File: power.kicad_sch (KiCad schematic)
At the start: 3 parts, among them U1 AP7363-33D-13

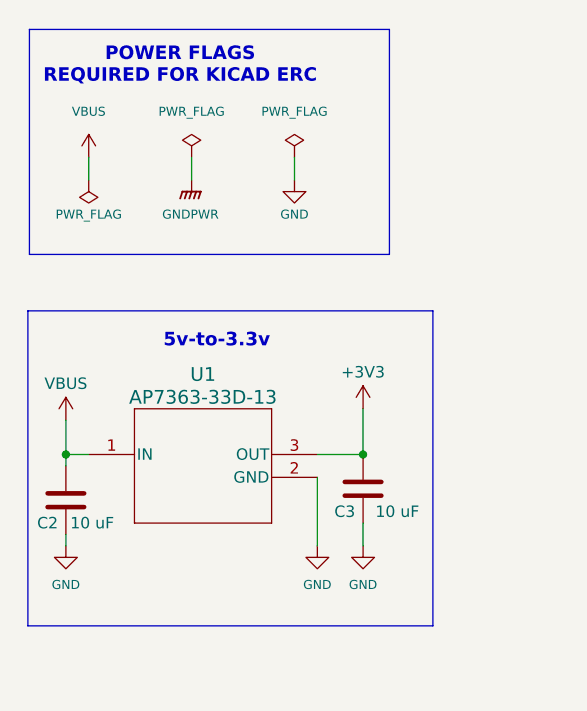
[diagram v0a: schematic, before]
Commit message: finished ERC, matched footprints, populated 3D models
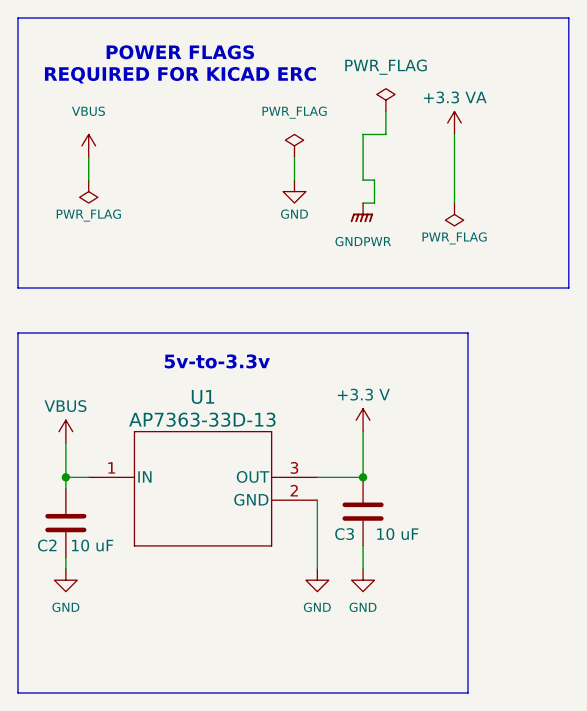
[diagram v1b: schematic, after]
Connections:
- net +3V3 renamed +3.3 V
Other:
- moved on the sheet: C2, C3, U1

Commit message: matched footprint name to name of component
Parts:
- U1: footprint AP7363_33D_13:TO252-3L_DIO -> AP7363_33D_13:AP7363-33D-13
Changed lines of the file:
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@@
 			)
 		)
-		(property "Footprint" "AP7363_33D_13:TO252-3L_DIO"
+		(property "Footprint" "AP7363_33D_13:AP7363-33D-13"
 			(at 12.446 69.088 0)
 			(effects

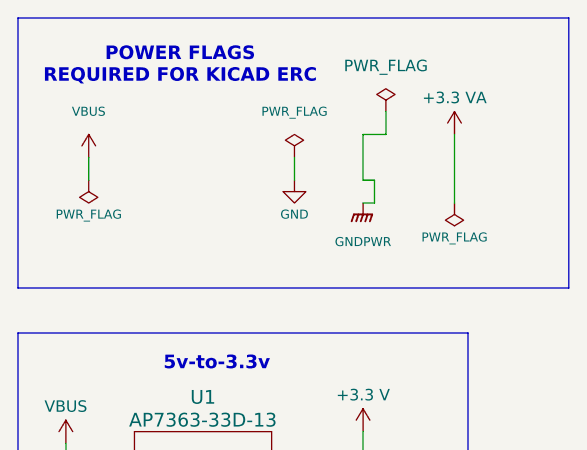
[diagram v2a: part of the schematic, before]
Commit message: removed manual switch
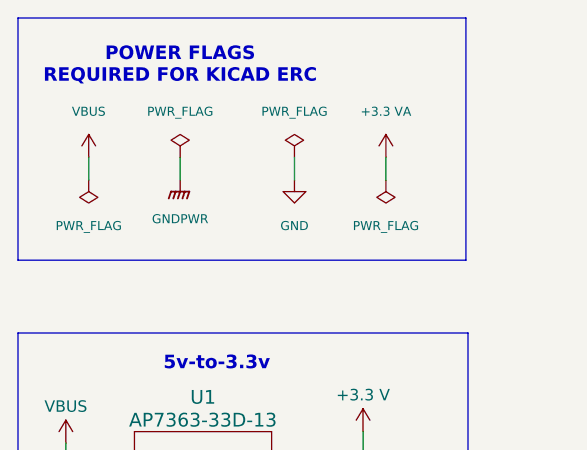
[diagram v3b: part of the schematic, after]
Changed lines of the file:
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@@
-	(wire
-		(pts
-			(xy 55.88 25.4) (xy 55.88 27.94)
-		)
-		(stroke
-			(width 0)
-			(type default)
-		)
-	)
-	(wire
-		(pts
-			(xy 53.34 35.56) (xy 54.61 35.56)
-		)
-		(stroke
-			(width 0)
-			(type default)
-		)
-	)
-	(wire
-		(pts
-			(xy 53.34 27.94) (xy 55.88 27.94)
-		)
-		(stroke
-			(width 0)
-			(type default)
-		)
-	)
 	(wire
 		(pts
@@
 	(wire
 		(pts
-			(xy 54.61 33.02) (xy 54.61 35.56)
-		)
-		(stroke
-			(width 0)
-			(type default)
-		)
-	)
-	(wire
-		(pts
-			(xy 53.34 33.02) (xy 53.34 27.94)
+			(xy 33.02 30.48) (xy 33.02 33.02)
 		)
 		(stroke
@@
 	(wire
 		(pts
-			(xy 54.61 33.02) (xy 53.34 33.02)
-		)
-		(stroke
-			(width 0)
-			(type default)
-		)
-	)
-	(wire
-		(pts
 			(xy 20.32 74.93) (xy 20.32 76.2)
 		)
@@
 	(wire
 		(pts
-			(xy 63.5 27.94) (xy 63.5 35.56)
+			(xy 55.88 30.48) (xy 55.88 33.02)
 		)
 		(stroke
@@
 	(rectangle
 		(start 15 15)
-		(end 76.2 45)
+		(end 64.77 41.91)
 		(stroke
 			(width 0)
@@
 	(symbol
 		(lib_id "power:GNDPWR")
-		(at 53.34 35.56 0)
+		(at 33.02 33.02 0)
 		(unit 1)
 		(exclude_from_sim no)
@@
 		(dnp no)
 		(property "Reference" "#PWR018"
-			(at 53.34 40.64 0)
+			(at 33.02 38.1 0)
 			(effects
 				(font
@@
 		)
 		(property "Value" "GNDPWR"
-			(at 53.34 39.878 0)
+			(at 33.02 37.338 0)
 			(effects
 				(font
@@
 		)
 		(property "Footprint" ""
-			(at 53.34 36.83 0)
+			(at 33.02 34.29 0)
 			(effects
 				(font
@@
 		)
 		(property "Datasheet" ""
-			(at 53.34 36.83 0)
+			(at 33.02 34.29 0)
 			(effects
 				(font
@@
 		)
 		(property "Description" "Power symbol creates a global label with name \"GNDPWR\" , global ground"
-			(at 53.34 35.56 0)
+			(at 33.02 33.02 0)
 			(effects
 				(font
@@
 	(symbol
 		(lib_id "power:+3V3")
-		(at 63.5 27.94 0)
+		(at 55.88 30.48 0)
 		(unit 1)
 		(exclude_from_sim no)
@@
 		(dnp no)
 		(property "Reference" "#PWR017"
-			(at 63.5 31.75 0)
+			(at 55.88 34.29 0)
 			(effects
 				(font
@@
 		)
 		(property "Value" "+3.3 VA"
-			(at 63.5 23.876 0)
-			(effects
-				(font
-					(size 1.27 1.27)
-				)
-			)
-		)
-		(property "Footprint" ""
-			(at 63.5 27.94 0)
+			(at 55.88 25.4 0)
+			(effects
+				(font
+					(size 1 1)
+				)
+			)
+		)
+		(property "Footprint" ""
+			(at 55.88 30.48 0)
 			(effects
 				(font
@@
 		)
 		(property "Datasheet" ""
-			(at 63.5 27.94 0)
+			(at 55.88 30.48 0)
 			(effects
 				(font
@@
 		)
 		(property "Description" "Power symbol creates a global label with name \"+3V3\""
-			(at 63.5 27.94 0)
+			(at 55.88 30.48 0)
 			(effects
 				(font
@@
 	(symbol
 		(lib_id "power:PWR_FLAG")
-		(at 55.88 25.4 0)
+		(at 33.02 30.48 0)
 		(unit 1)
 		(exclude_from_sim no)
@@
 		(fields_autoplaced yes)
 		(property "Reference" "#FLG01"
-			(at 55.88 23.495 0)
+			(at 33.02 28.575 0)
 			(effects
 				(font
@@
 		)
 		(property "Value" "PWR_FLAG"
-			(at 55.88 20.32 0)
-			(effects
-				(font
-					(size 1.27 1.27)
-				)
-			)
-		)
-		(property "Footprint" ""
-			(at 55.88 25.4 0)
+			(at 33.02 25.4 0)
+			(effects
+				(font
+					(size 1 1)
+				)
+			)
+		)
+		(property "Footprint" ""
+			(at 33.02 30.48 0)
 			(effects
 				(font
@@
 		)
 		(property "Datasheet" "~"
-			(at 55.88 25.4 0)
+			(at 33.02 30.48 0)
 			(effects
 				(font
@@
 		)
 		(property "Description" "Special symbol for telling ERC where power comes from"
-			(at 55.88 25.4 0)
+			(at 33.02 30.48 0)
 			(effects
 				(font
@@
 		)
 		(property "Value" "PWR_FLAG"
-			(at 22.86 36.83 0)
+			(at 22.86 38.1 0)
 			(effects
 				(font
@@
 		)
 		(property "Value" "GND"
-			(at 45.72 36.83 0)
+			(at 45.72 38.1 0)
 			(effects
 				(font
@@
 	(symbol
 		(lib_id "power:PWR_FLAG")
-		(at 63.5 35.56 180)
+		(at 55.88 33.02 180)
 		(unit 1)
 		(exclude_from_sim no)
@@
 		(dnp no)
 		(property "Reference" "#FLG02"
-			(at 63.5 37.465 0)
+			(at 55.88 34.925 0)
 			(effects
 				(font
@@
 		)
 		(property "Value" "PWR_FLAG"
-			(at 63.5 39.37 0)
+			(at 55.88 38.1 0)
 			(effects
 				(font
@@
 		)
 		(property "Footprint" ""
-			(at 63.5 35.56 0)
+			(at 55.88 33.02 0)
 			(effects
 				(font
@@
 		)
 		(property "Datasheet" "~"
-			(at 63.5 35.56 0)
+			(at 55.88 33.02 0)
 			(effects
 				(font
@@
 		)
 		(property "Description" "Special symbol for telling ERC where power comes from"
-			(at 63.5 35.56 0)
-			(effects
-				(font
+			(at 55.88 33.02 0)
+			(effects
+				(font

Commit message: added diode
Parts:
- added CR2, CR3: SD2010S040S3R0, SDO_KAVX_KAV, symbol DIO_Schoktty_40V:SD2010S040S3R0
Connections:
- net +3.3 V: now also CR2.2, CR3.2
- new net VBOARD: CR3.1
- new net VMCU: CR2.1
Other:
- note added: "3.3v-to-MCU"
- note added: "3.3v-to-VBOARD"

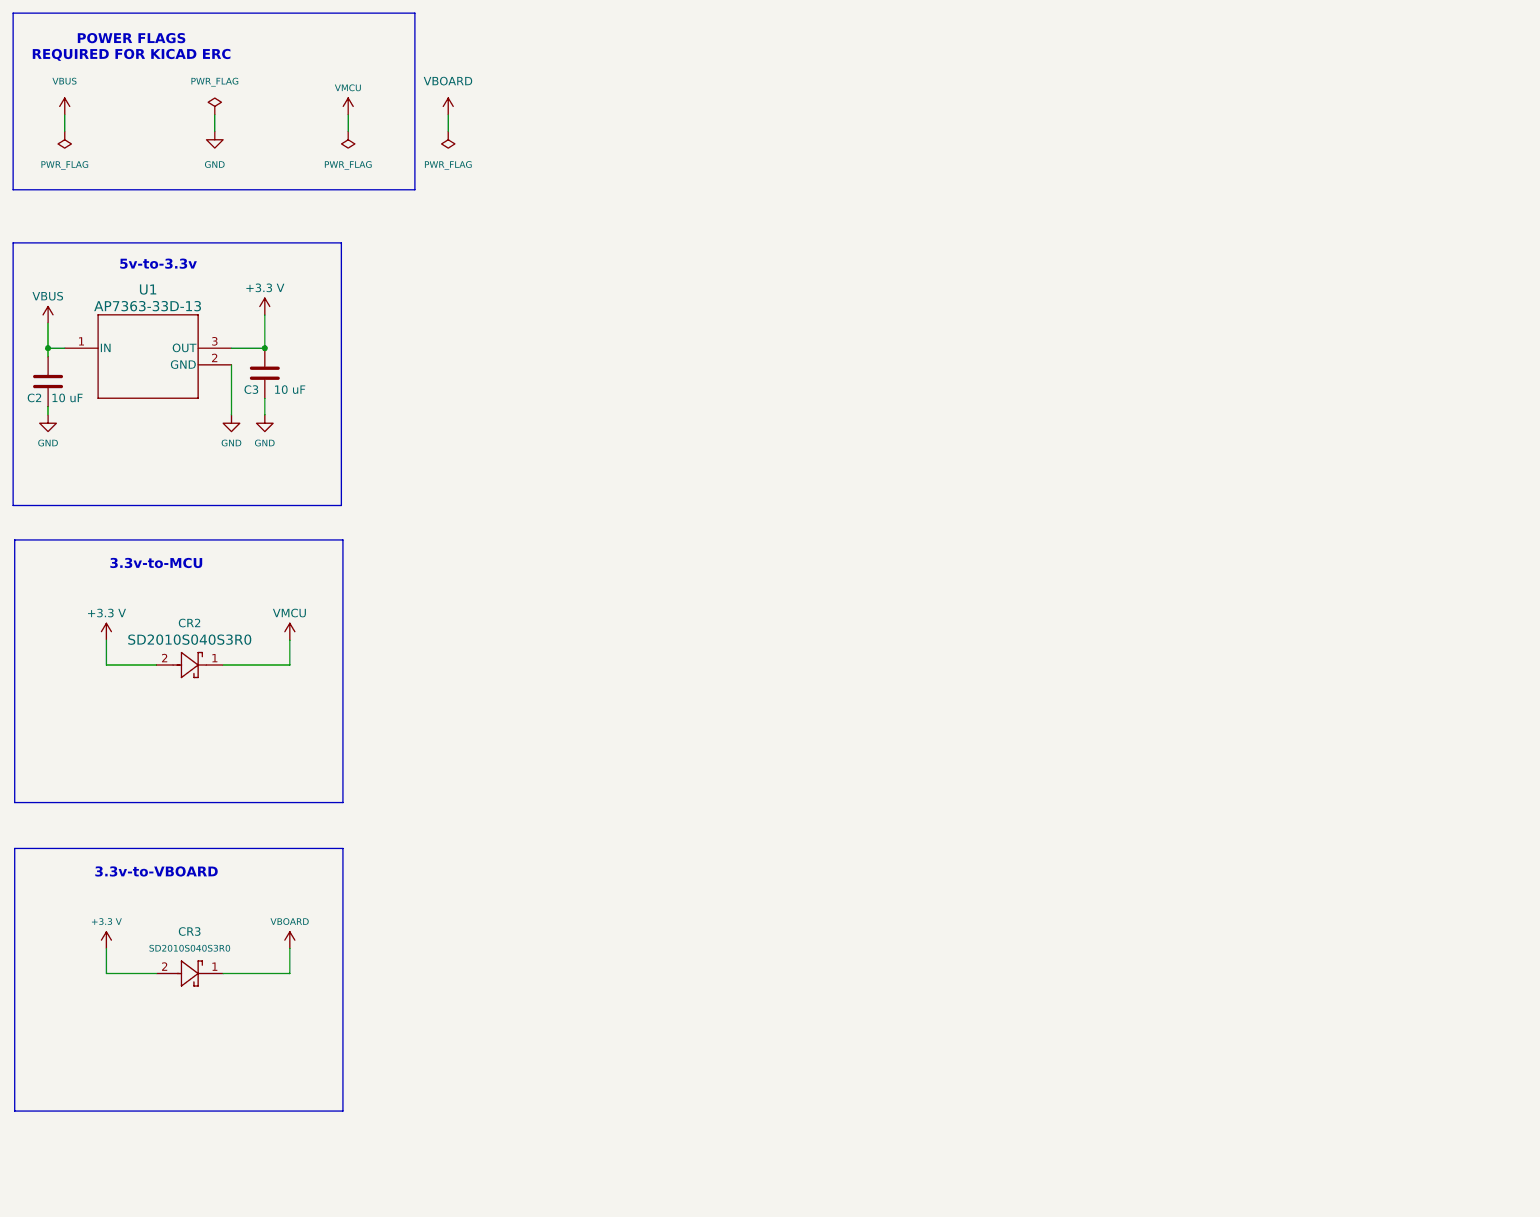
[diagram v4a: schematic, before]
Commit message: separated voltage source labels
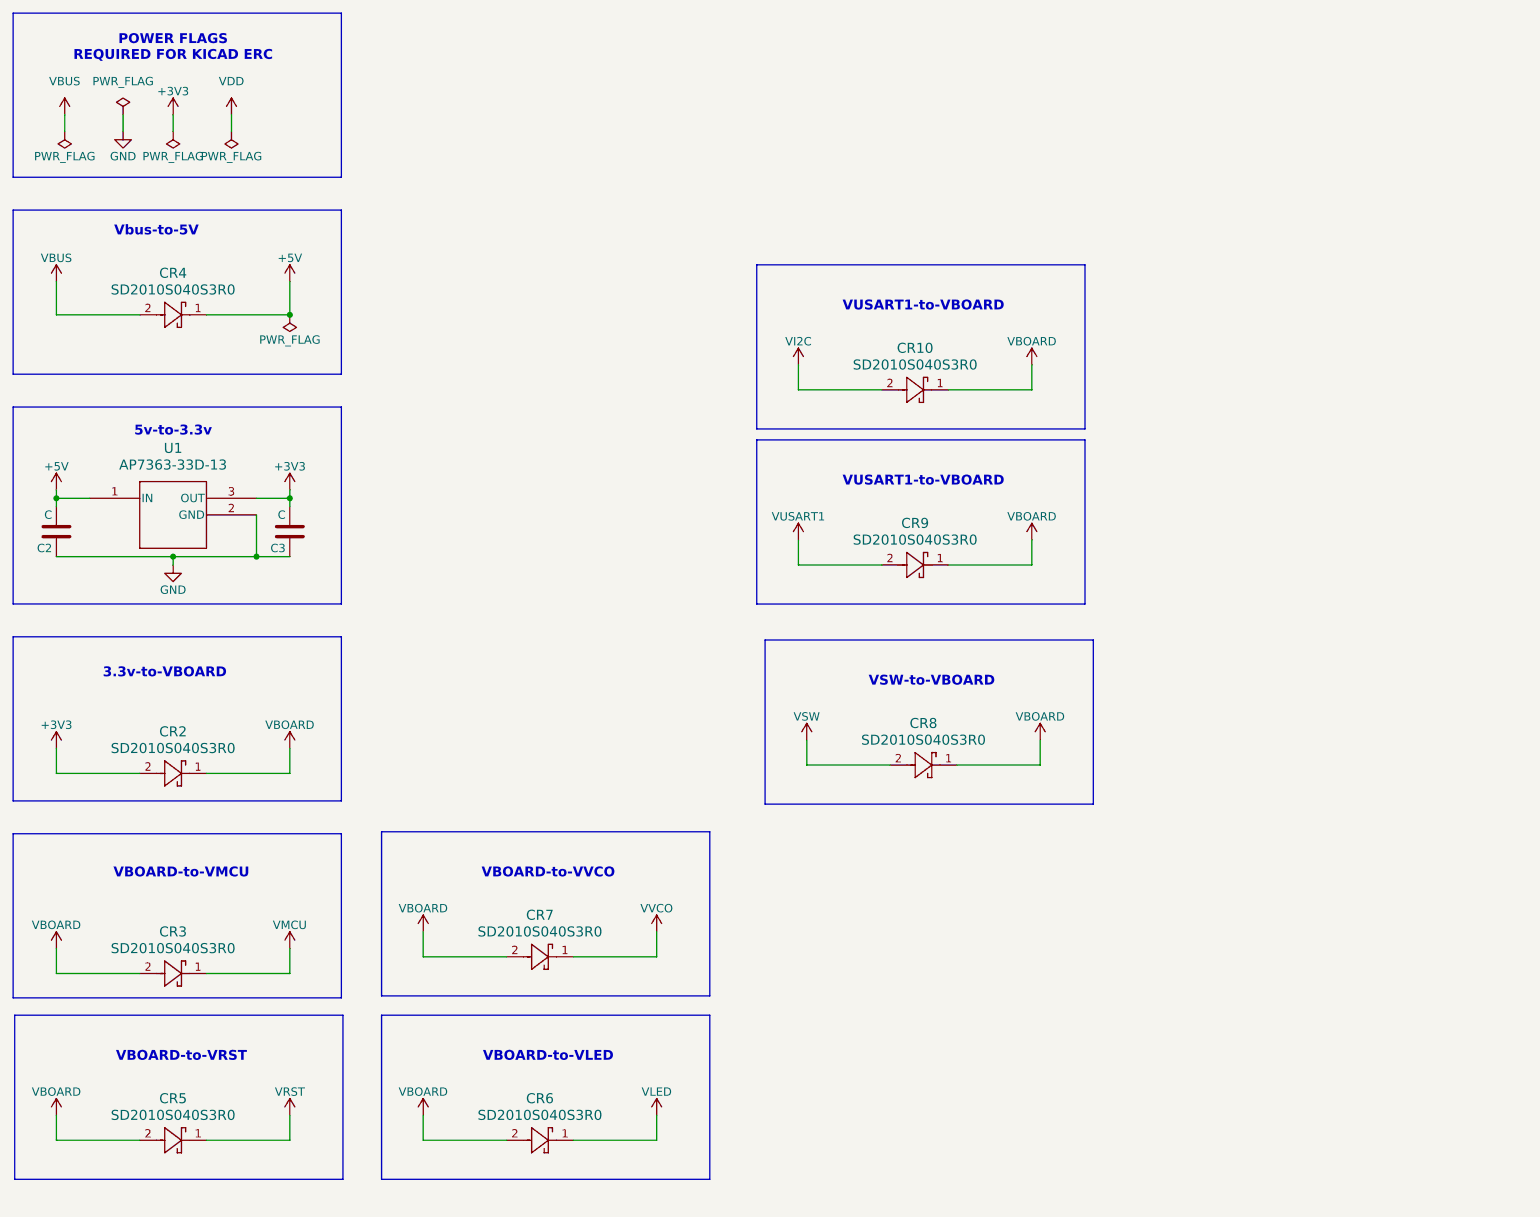
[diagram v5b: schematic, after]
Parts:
- added CR10, CR4, CR5, CR6, CR7, CR8, CR9: SD2010S040S3R0, SDO_KAVX_KAV, symbol DIO_Schoktty_40V:SD2010S040S3R0
- C2, C3: value 10 uF -> C
- U1: footprint AP7363_33D_13:AP7363-33D-13 -> TO252-3L_DIO; symbol AP7363_33D_13:AP7363-33D-13 -> PMIC_LDO_3.3V:AP7363-33D-13
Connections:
- net VBOARD: now also CR2.1, CR3.2, CR10.1, CR5.2, CR6.2, CR7.2, CR8.1, CR9.1; no longer CR3.1
- net VBUS: now also CR4.2; no longer C2.2, U1.1 (IN)
- net VMCU: now also CR3.1; no longer CR2.1
- net +3.3 V renamed +3V3
- net +3V3: no longer CR3.2
- new net +5V: C2.2, CR4.1, U1.1 (IN)
- new net VI2C: CR10.2
- new net VLED: CR6.1
- new net VRST: CR5.1
- new net VSW: CR8.2
- new net VUSART1: CR9.2
- new net VVCO: CR7.1
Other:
- note added: "VBOARD-to-VLED"
- note added: "VBOARD-to-VMCU"
- note added: "VBOARD-to-VRST"
- note added: "VBOARD-to-VVCO"
- note added: "VSW-to-VBOARD"
- note added: "VUSART1-to-VBOARD"
- note added: "Vbus-to-5V"
- note removed: "3.3v-to-MCU"
- moved on the sheet: C2, C3, CR2, CR3, U1

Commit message: isolated v sources
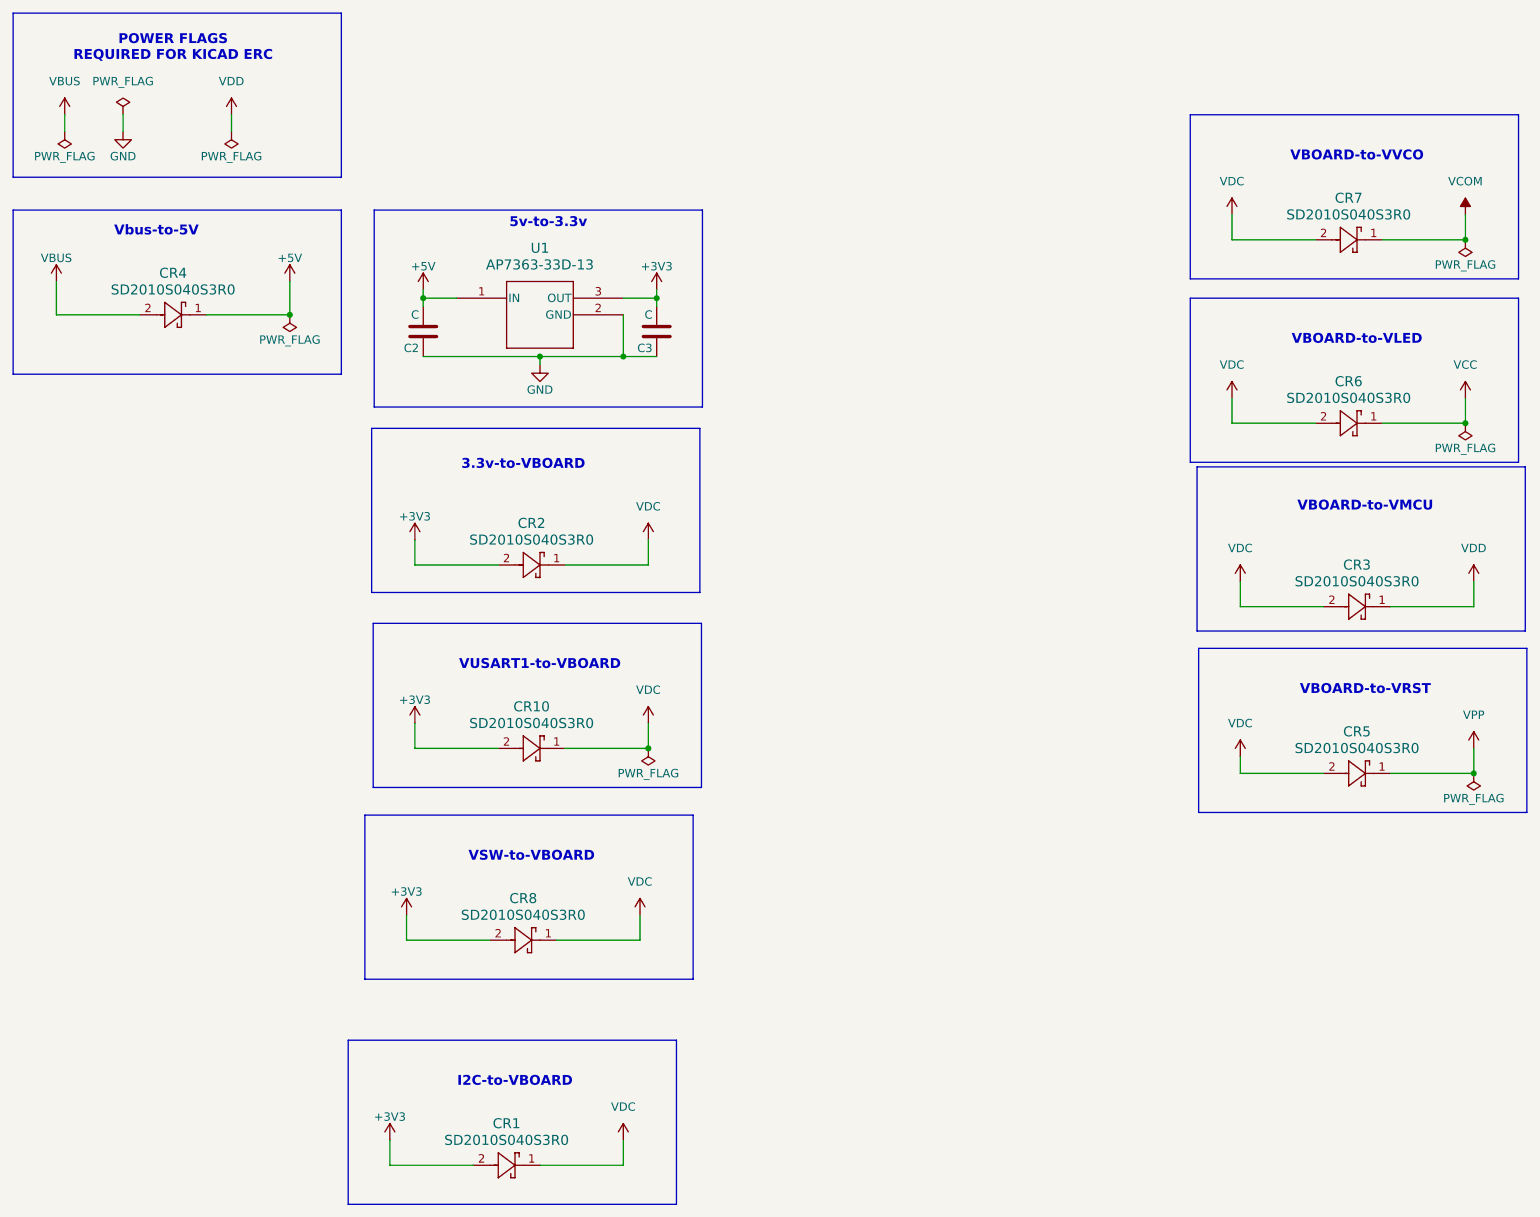
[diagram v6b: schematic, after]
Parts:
- removed CR9: SD2010S040S3R0, SDO_KAVX_KAV, symbol DIO_Schoktty_40V:SD2010S040S3R0
- added CR1: SD2010S040S3R0, SDO_KAVX_KAV, symbol DIO_Schoktty_40V:SD2010S040S3R0
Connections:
- net VI2C is gone; now on net +3V3: CR10.2
- net VMCU is gone; now on net VDD: CR3.1
- net VSW is gone; now on net +3V3: CR8.2
- net +3V3: now also CR1.2
- net VBOARD renamed VDC
- net VDC: now also CR1.1
- net VLED renamed VCC
- net VRST renamed VPP
- net VVCO renamed VCOM
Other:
- note added: "I2C-to-VBOARD"
- moved on the sheet: C2, C3, CR10, CR2, CR3, CR5, CR6, CR7, CR8, U1

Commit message: added sheets
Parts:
- CR1, CR10, CR2, CR3, CR4, CR5, CR6, CR7, CR8: footprint SDO_KAVX_KAV -> DIODE_SCHOTTKY_40V_3A:SDO_KAVX_KAV
- U1: footprint TO252-3L_DIO -> PMIC_VREG_LDO_3.3V:TO252-3L_DIO
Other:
- note added: "Reset Ground Share"
- moved on the sheet: C2, C3, CR1, CR10, CR2, CR3, CR5, CR6, CR7, CR8, U1
